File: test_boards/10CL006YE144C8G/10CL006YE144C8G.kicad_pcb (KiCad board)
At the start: 2 copper layers, 88 parts, among them IC1 10CL006YE144C8G, J1 CL_JTAG, U1 W25Q128JVS, Y1 SG-7050CAN

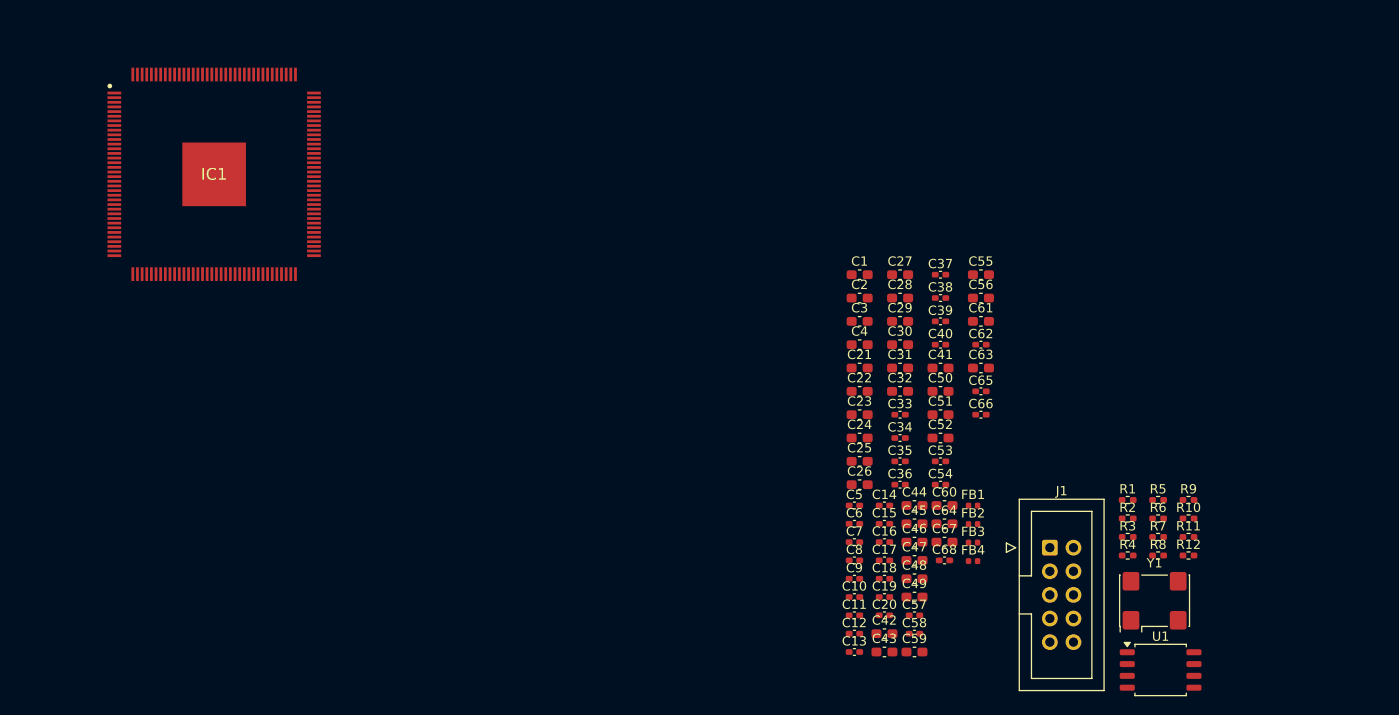
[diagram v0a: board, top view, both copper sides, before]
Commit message: Добавлен экстрактор выделенных участков в качестве шаблона
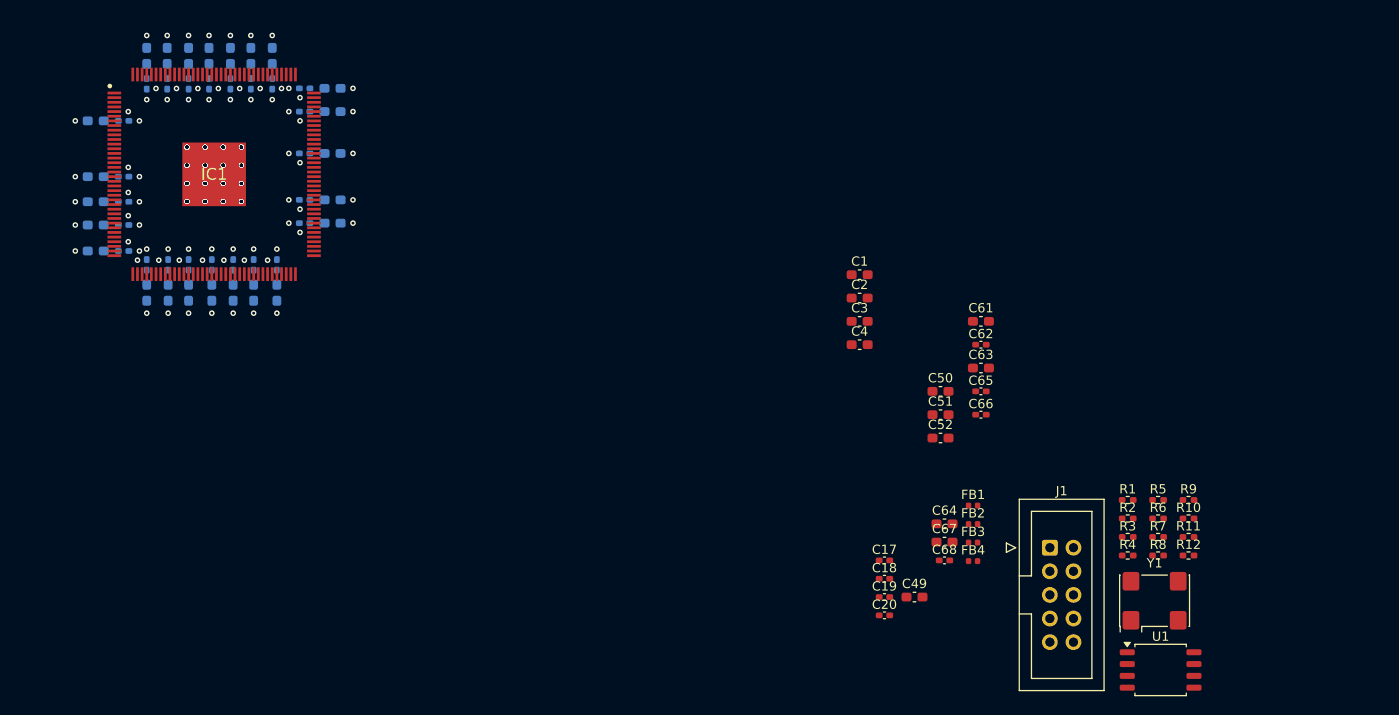
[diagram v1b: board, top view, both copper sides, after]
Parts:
- C10, C11, C12, C13, C14, C15, C16, C21, C22, C23, C24, C25, C26, C27, C28, C29, C30, C31, C32, C33, C34, C35, C36, C37, C38, C39, C40, C41, C42, C43, C44, C45, C46, C47, C48, C5, C53, C54, C55, C56, C57, C58, C59, C6, C60, C7, C8, C9: moved to B.Cu
- moved C48 98.1 mm to (72.5, 68.9), turned to 90 degrees
- moved C59 98.1 mm to (64.8, 89.9), turned to 180 degrees
- moved C42 95.6 mm to (64.8, 87.1), turned to 180 degrees
- moved C41 94.7 mm to (64.8, 75.9), turned to 180 degrees
- moved C57 93.7 mm to (67.8, 89.9)
- moved C16 93.4 mm to (70.3, 71.9), turned to -90 degrees
- moved C13 90.8 mm to (79.3, 71.9), turned to -90 degrees
- moved C55 89.8 mm to (70.3, 94.3), turned to -90 degrees
- moved C47 89.7 mm to (81.5, 68.9), turned to 90 degrees
- moved C33 89.3 mm to (67.8, 75.9)
- moved C32 88.7 mm to (70.3, 68.9), turned to 90 degrees
- moved C15 88.6 mm to (74.8, 71.9), turned to -90 degrees
- moved C58 88.0 mm to (87.3, 72.4), turned to 180 degrees
- moved C53 88.0 mm to (70.3, 91.3), turned to 90 degrees
- moved C40 87.8 mm to (72.5, 71.9), turned to -90 degrees
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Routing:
- net GND: vias 0 -> 352
- net +3V3_VCCIO: vias 0 -> 12
- net +2V5_VCCA: vias 0 -> 2
- net +1V2_VCCINT: vias 0 -> 8
- net +1V2_VCCD_PLL: vias 0 -> 2

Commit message: Добавлено две тестовых платы
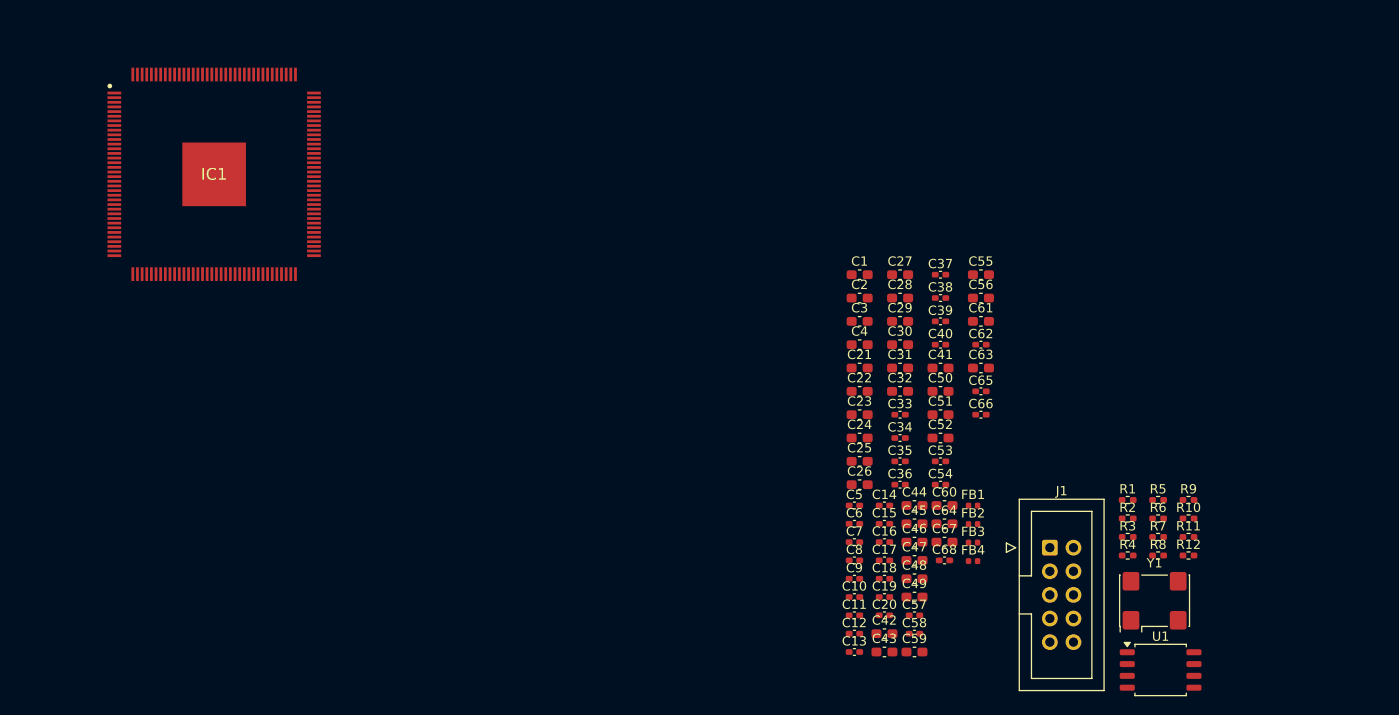
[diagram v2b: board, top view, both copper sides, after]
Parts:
- C10, C11, C12, C13, C14, C15, C16, C21, C22, C23, C24, C25, C26, C27, C28, C29, C30, C31, C32, C33, C34, C35, C36, C37, C38, C39, C40, C41, C42, C43, C44, C45, C46, C47, C48, C5, C53, C54, C55, C56, C57, C58, C59, C6, C60, C7, C8, C9: moved to F.Cu
- moved C48 98.1 mm to (152.9, 125.1), turned to 0 degrees
- moved C59 98.1 mm to (152.9, 133.0), turned to 0 degrees
- moved C42 95.6 mm to (149.7, 131.0), turned to 0 degrees
- moved C41 94.7 mm to (155.7, 102.4), turned to 0 degrees
- moved C57 93.7 mm to (152.9, 129.1)
- moved C16 93.4 mm to (149.7, 121.2), turned to 0 degrees
- moved C13 90.8 mm to (146.4, 133.0), turned to 0 degrees
- moved C55 89.8 mm to (160.1, 92.4), turned to 0 degrees
- moved C47 89.7 mm to (152.9, 123.1), turned to 0 degrees
- moved C33 89.3 mm to (151.4, 107.5)
- moved C32 88.7 mm to (151.4, 105.0), turned to 0 degrees
- moved C15 88.6 mm to (149.7, 119.2), turned to 0 degrees
- moved C58 88.0 mm to (152.9, 131.0), turned to 0 degrees
- moved C53 88.0 mm to (155.7, 112.5), turned to 0 degrees
- moved C40 87.8 mm to (155.7, 99.9), turned to 0 degrees
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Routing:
- net GND: vias 352 -> 0
- net +3V3_VCCIO: vias 12 -> 0
- net +2V5_VCCA: vias 2 -> 0
- net +1V2_VCCINT: vias 8 -> 0
- net +1V2_VCCD_PLL: vias 2 -> 0

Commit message: Добавлен скрипт диагностиги падения KiCad
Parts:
- moved C1 38.9 mm to (116.2, 116.1), turned to -90 degrees
- moved FB1 38.8 mm to (120.4, 115.2)
- moved C49 34.1 mm to (120.0, 117.9), turned to 180 degrees
- moved C17 32.1 mm to (118.4, 115.8), turned to -90 degrees
- moved C2 2.88 mm to (144.1, 94.9)
- moved C5 0.31 mm to (146.5, 117.5)
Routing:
- net +1V2: track 0.00 -> 5.13 mm, vias 0 -> 1
- net GND: track 0.00 -> 3.12 mm, vias 0 -> 3
- net +1V2_VCCINT: track 0.00 -> 2.64 mm

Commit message: Правки документации
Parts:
- C10, C11, C12, C13, C14, C15, C16, C21, C22, C23, C24, C25, C26, C27, C28, C29, C30, C31, C32, C33, C34, C35, C36, C37, C38, C39, C40, C41, C42, C43, C44, C45, C46, C47, C48, C5, C53, C54, C55, C56, C57, C58, C59, C6, C60, C7, C8, C9: moved to B.Cu
- moved FB4 111.4 mm to (62.4, 68.0)
- moved C20 107.8 mm to (60.5, 68.6), turned to -90 degrees
- moved C52 101.6 mm to (62.1, 70.7), turned to 180 degrees
- moved C48 98.1 mm to (72.5, 68.9), turned to 90 degrees
- moved C59 98.1 mm to (64.8, 89.9), turned to 180 degrees
- moved C42 95.6 mm to (64.8, 87.1), turned to 180 degrees
- moved C41 94.7 mm to (64.8, 75.9), turned to 180 degrees
- moved C4 94.1 mm to (58.2, 68.9), turned to -90 degrees
- moved C57 93.7 mm to (67.8, 89.9)
- moved C16 93.4 mm to (70.3, 71.9), turned to -90 degrees
- moved C13 90.8 mm to (79.3, 71.9), turned to -90 degrees
- moved C55 89.8 mm to (70.3, 94.3), turned to -90 degrees
- moved C47 89.7 mm to (81.5, 68.9), turned to 90 degrees
- moved C33 89.3 mm to (67.8, 75.9)
- moved C32 88.7 mm to (70.3, 68.9), turned to 90 degrees
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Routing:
- net GND: vias 3 -> 22
- net +3V3: vias 0 -> 1

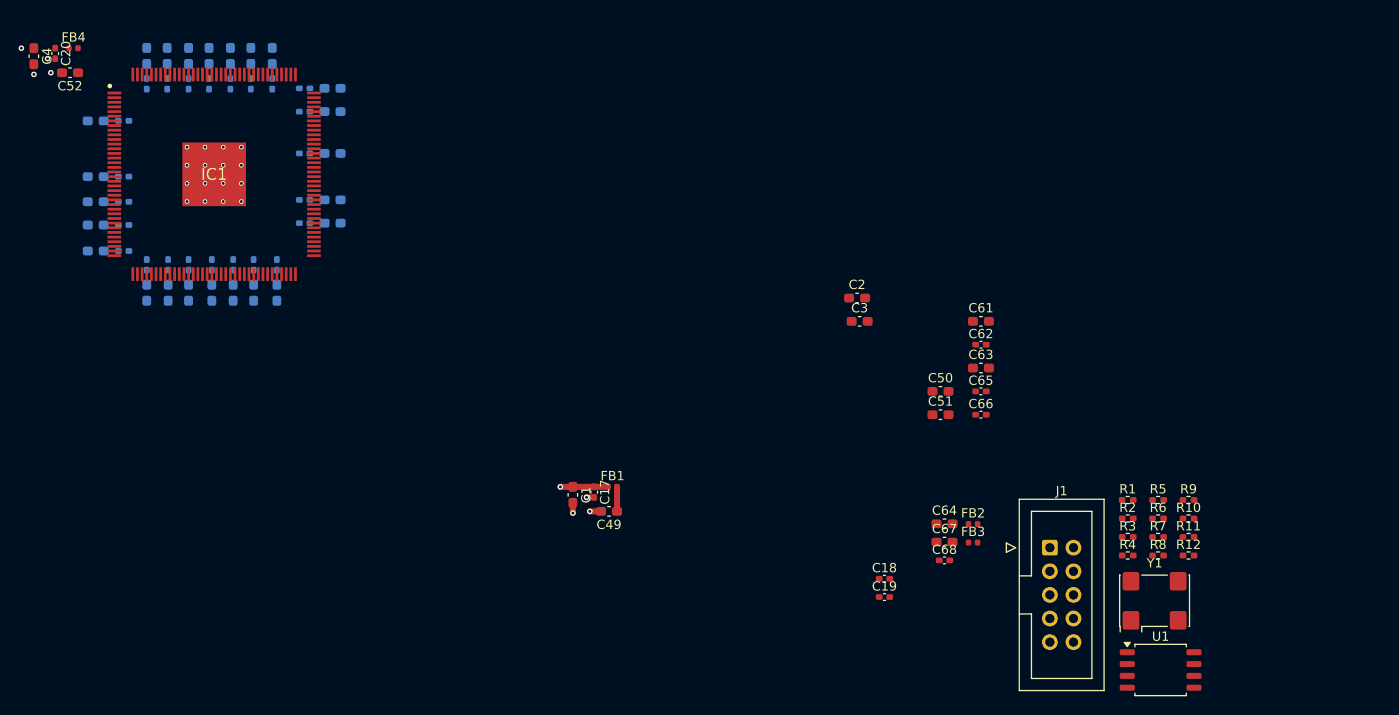
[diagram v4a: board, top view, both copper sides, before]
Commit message: Упразднение глобальных target_ref и side
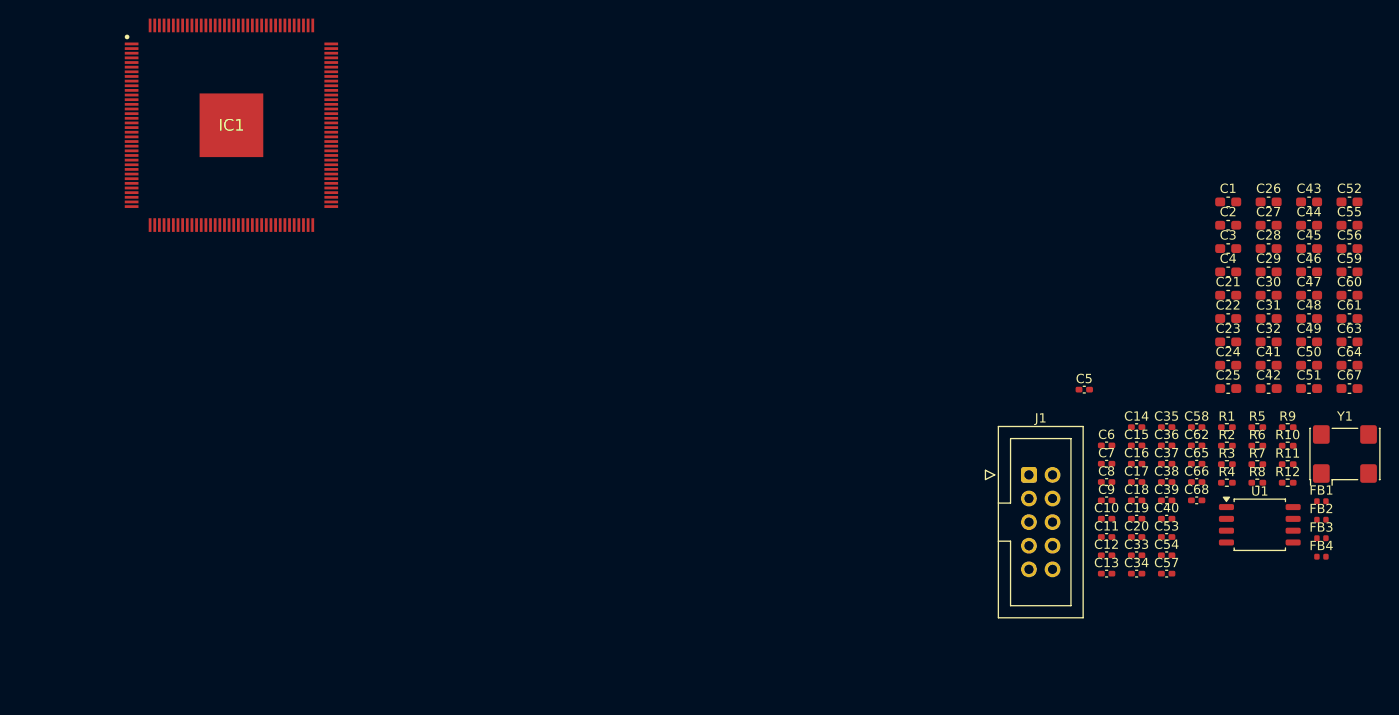
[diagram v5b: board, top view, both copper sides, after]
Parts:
- C10, C11, C12, C13, C14, C15, C16, C21, C22, C23, C24, C25, C26, C27, C28, C29, C30, C31, C32, C33, C34, C35, C36, C37, C38, C39, C40, C41, C42, C43, C44, C45, C46, C47, C48, C5, C53, C54, C55, C56, C57, C58, C59, C6, C60, C7, C8, C9: moved to F.Cu
- moved FB4 145.0 mm to (196.7, 122.7)
- moved C52 138.4 mm to (199.7, 84.6), turned to 0 degrees
- moved C59 134.9 mm to (199.7, 92.1), turned to 0 degrees
- moved C4 130.6 mm to (186.7, 92.1), turned to 0 degrees
- moved C55 129.6 mm to (199.7, 87.1), turned to 0 degrees
- moved C41 128.9 mm to (191.0, 102.1), turned to 0 degrees
- moved C20 127.4 mm to (176.8, 120.6), turned to 0 degrees
- moved C42 127.4 mm to (191.0, 104.7), turned to 0 degrees
- moved C48 126.1 mm to (195.4, 97.1), turned to 0 degrees
- moved C32 124.6 mm to (191.0, 99.6), turned to 0 degrees
- moved C21 122.5 mm to (186.7, 94.6), turned to 0 degrees
- moved C22 122.5 mm to (186.7, 97.1), turned to 0 degrees
- moved C43 120.9 mm to (195.4, 84.6), turned to 0 degrees
- moved C31 119.6 mm to (191.0, 97.1), turned to 0 degrees
- moved C33 118.6 mm to (176.8, 122.6)
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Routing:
- net +1V2: track 5.13 -> 0.00 mm, vias 1 -> 0
- net GND: track 3.12 -> 0.00 mm, vias 22 -> 0
- net +1V2_VCCINT: track 2.64 -> 0.00 mm
- net +3V3: vias 1 -> 0

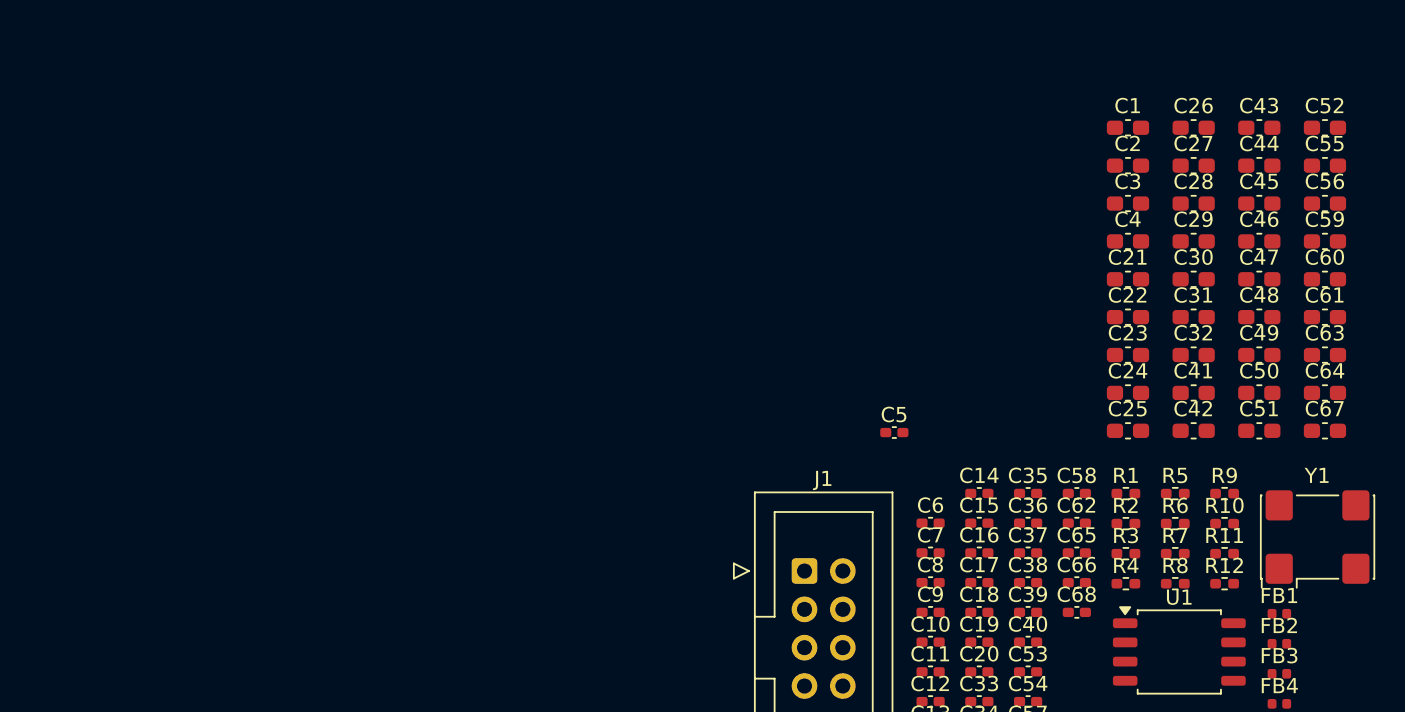
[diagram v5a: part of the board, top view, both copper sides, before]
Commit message: добавлено извлечение шаблона с 0 относительно via. Поправил регистр действий. Теперь ищутся реальные компоненты на плате
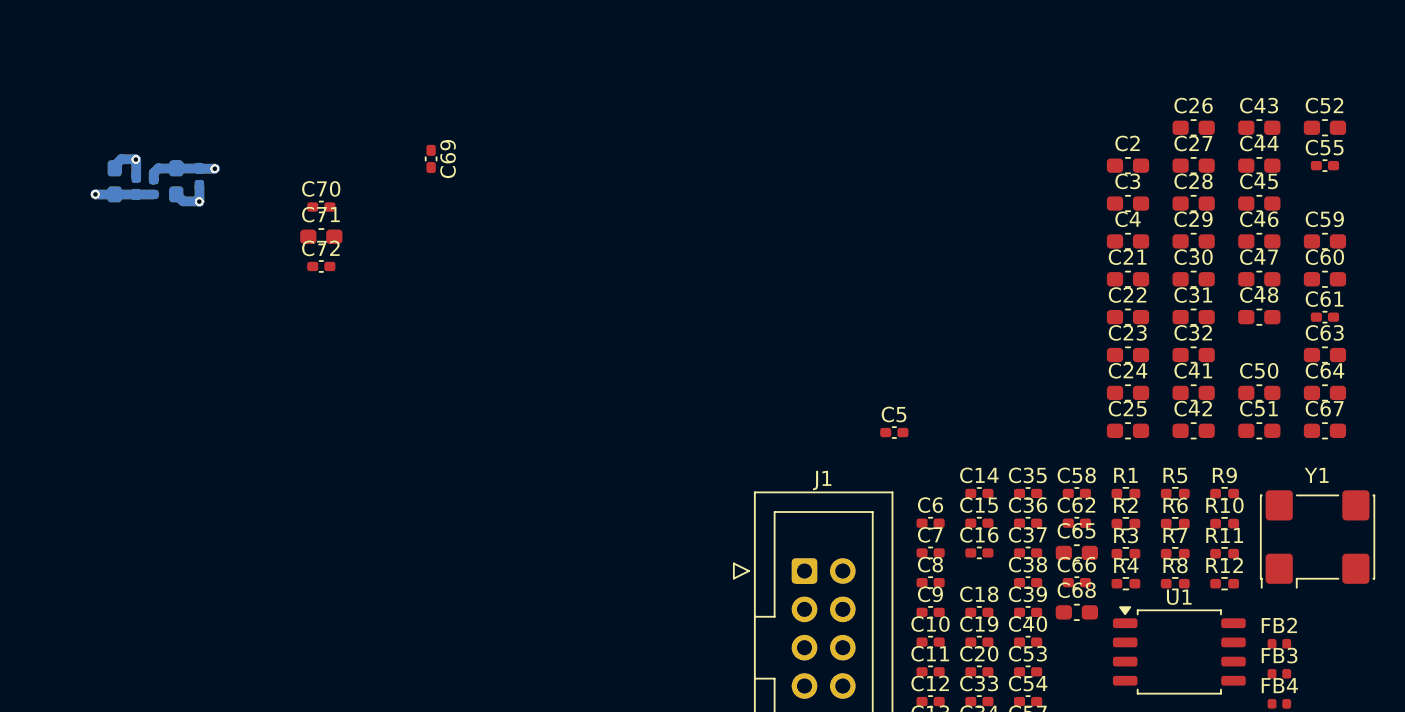
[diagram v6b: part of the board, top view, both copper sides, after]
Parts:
- added C69: 100 nF, Capacitor_SMD:C_0402_1005Metric_Pad0.74x0.62mm_HandSolder, F.Cu at (140.5, 86.6)
- added C70: 100 nF, Capacitor_SMD:C_0402_1005Metric_Pad0.74x0.62mm_HandSolder, F.Cu at (133.2, 89.8)
- added C71: 1uF, Capacitor_SMD:C_0603_1608Metric_Pad1.08x0.95mm_HandSolder, F.Cu at (133.2, 91.8)
- added C72: 100 nF, Capacitor_SMD:C_0402_1005Metric_Pad0.74x0.62mm_HandSolder, F.Cu at (133.2, 93.8)
- C1, C17, C49, FB1: moved to B.Cu
- C55: value 4.7 uF -> 100 nF; footprint Capacitor_SMD:C_0603_1608Metric_Pad1.08x0.95mm_HandSolder -> Capacitor_SMD:C_0402_1005Metric_Pad0.74x0.62mm_HandSolder
- C56: value 4.7 uF -> 100 nF; footprint Capacitor_SMD:C_0603_1608Metric_Pad1.08x0.95mm_HandSolder -> Capacitor_SMD:C_0402_1005Metric_Pad0.74x0.62mm_HandSolder; moved to B.Cu
- C61: value 1uF -> 100 nF; footprint Capacitor_SMD:C_0603_1608Metric_Pad1.08x0.95mm_HandSolder -> Capacitor_SMD:C_0402_1005Metric_Pad0.74x0.62mm_HandSolder
- C63, C64: value 1uF -> 4.7 uF
- C65, C68: value 100 nF -> 1uF; footprint Capacitor_SMD:C_0402_1005Metric_Pad0.74x0.62mm_HandSolder -> Capacitor_SMD:C_0603_1608Metric_Pad1.08x0.95mm_HandSolder
- moved FB1 79.8 mm to (122.1, 88.5), turned to 90 degrees
- moved C56 74.6 mm to (125.1, 87.8), turned to -90 degrees
- moved C49 72.7 mm to (123.6, 88.1), turned to -90 degrees
- moved C1 67.2 mm to (119.5, 88.1), turned to 90 degrees
- moved C17 61.7 mm to (120.9, 88.4), turned to 90 degrees
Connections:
- C56 pad 1: +1V2_VCCD_PLL -> +1V2_VCCINT
- C58 pad 1: +2V5_VCCA -> +3V3_VCCIO
- C59 pad 1: +2V5_VCCA -> +1V2_VCCD_PLL
- C60 pad 1: +2V5_VCCA -> +1V2_VCCD_PLL
- C61 pad 1: +3V3 -> +2V5_VCCA
- C62 pad 1: +3V3 -> +2V5_VCCA
- C63 pad 1: +3V3 -> +2V5_VCCA
- C64 pad 1: +3V3_OSCILL -> +2V5_VCCA
- C66 pad 1: GND -> +3V3
- C66 pad 2: +3V3_OSCILL -> GND
- C67 pad 1: +3V3_FLASH -> +3V3
- C68 pad 1: GND -> +3V3_OSCILL
- C68 pad 2: +3V3_FLASH -> GND
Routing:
- net GND: track 0.00 -> 5.72 mm, vias 0 -> 2
- net +1V2_VCCINT: track 0.00 -> 4.63 mm, vias 0 -> 1
- net +1V2: track 0.00 -> 3.86 mm, vias 0 -> 1

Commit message: Исправлен баг планнера -- не размещал на нужной стороне детали. Добавлен приоритет размещения деталей (клонирование) по выделению
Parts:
- C1, C17, C49, C56, FB1: moved to F.Cu
- moved C56 74.6 mm to (199.7, 89.6), turned to 0 degrees
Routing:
- net GND: track 5.72 -> 0.00 mm, vias 2 -> 0
- net +1V2_VCCINT: track 4.63 -> 0.00 mm, vias 1 -> 0
- net +1V2: track 3.86 -> 0.00 mm, vias 1 -> 0
